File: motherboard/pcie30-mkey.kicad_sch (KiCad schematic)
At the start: 58 parts, among them IC1 PI6C557-05BLE, J15 Bus_M.2_Socket_M, U20 TPS54331DR, U21 AP2127K-3.3, Y1 25MHz

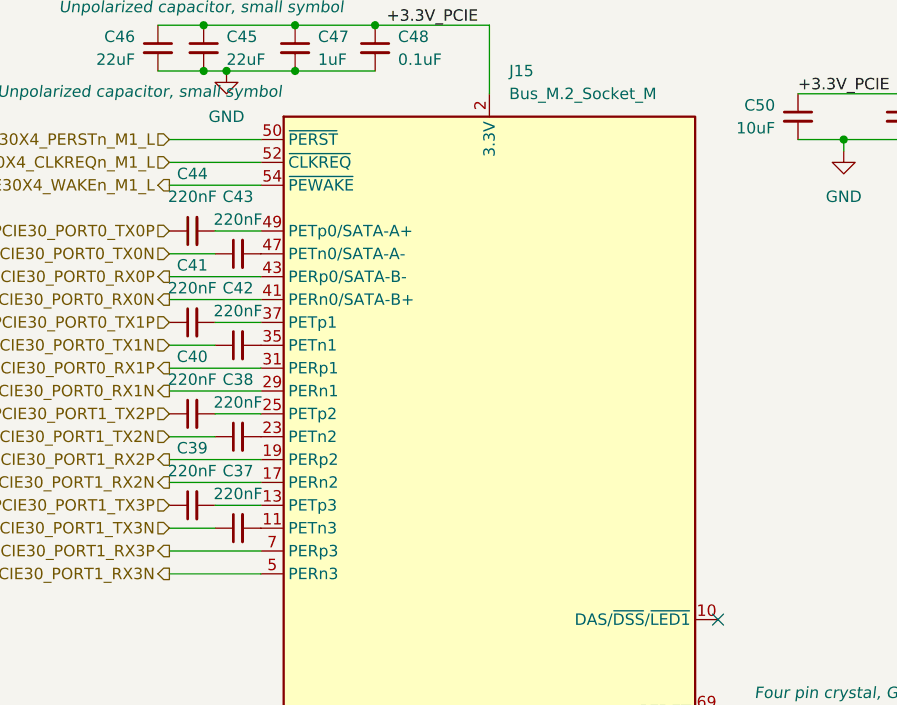
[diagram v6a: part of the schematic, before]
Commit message: placement roughly halfway done
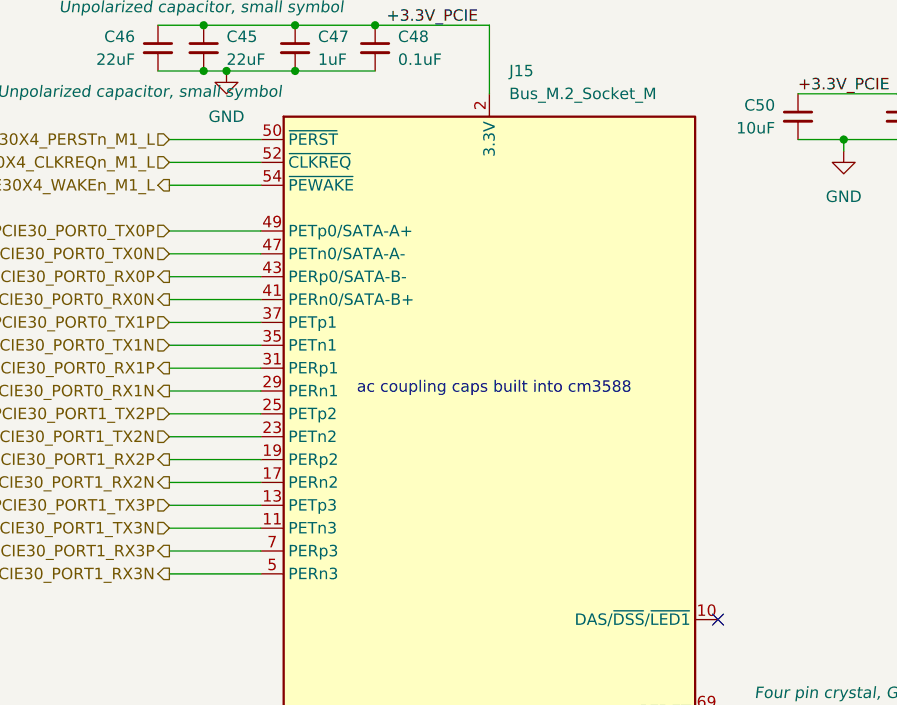
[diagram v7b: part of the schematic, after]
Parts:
- removed C37, C38, C39, C40, C41, C42, C43, C44: 220nF, Capacitor_SMD:C_0402_1005Metric, symbol Device:C_Small
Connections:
- net PCIE30_PORT0_TX0N: now also J15.47 (PETn0/SATA-A-)
- net PCIE30_PORT0_TX0P: now also J15.49 (PETp0/SATA-A+)
- net PCIE30_PORT0_TX1N: now also J15.35 (PETn1)
- net PCIE30_PORT0_TX1P: now also J15.37 (PETp1)
- net PCIE30_PORT1_TX2N: now also J15.23 (PETn2)
- net PCIE30_PORT1_TX2P: now also J15.25 (PETp2)
- net PCIE30_PORT1_TX3N: now also J15.11 (PETn3)
- net PCIE30_PORT1_TX3P: now also J15.13 (PETp3)
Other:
- note added: "ac coupling caps built into cm3588"

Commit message: layout nearing completion
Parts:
- C50, C52, C69: footprint Capacitor_SMD:C_0402_1005Metric -> Capacitor_SMD:C_0603_1608Metric
- IC1: footprint SOP65P640X120-20N -> SOP65P640X120-20N:SOP65P640X120-20N
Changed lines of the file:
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@@
 			)
 		)
-		(property "Footprint" "Capacitor_SMD:C_0402_1005Metric"
+		(property "Footprint" "Capacitor_SMD:C_0603_1608Metric"
 			(at 168.91 41.91 0)
 			(effects
@@
 		)
 		(property "Description" "Four pin crystal, GND on pins 2 and 4, small symbol"
-			(at 139.7 94.488 0)
+			(at 139.192 89.662 0)
 			(effects
 				(font
@@
 		(on_board yes)
 		(dnp no)
-		(fields_autoplaced yes)
 		(property "Reference" "C50"
 			(at 119.38 29.2162 0)
@@
 			)
 		)
-		(property "Footprint" "Capacitor_SMD:C_0402_1005Metric"
+		(property "Footprint" "Capacitor_SMD:C_0603_1608Metric"
 			(at 121.92 30.48 0)
 			(effects
@@
 			)
 		)
-		(property "Footprint" "SOP65P640X120-20N"
+		(property "Footprint" "SOP65P640X120-20N:SOP65P640X120-20N"
 			(at 204.47 160.96 0)
 			(effects
@@
 			)
 		)
-		(property "Footprint" "Capacitor_SMD:C_0402_1005Metric"
+		(property "Footprint" "Capacitor_SMD:C_0603_1608Metric"
 			(at 165.1 41.91 0)
 			(effects
